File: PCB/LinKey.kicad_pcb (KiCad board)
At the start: 2 copper layers, 25 x 43.5 mm, 1 part

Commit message: Release PCB v1
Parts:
- added C1: 2,2u, Capacitor_SMD:C_0805_2012Metric_Pad1.18x1.45mm_HandSolder, F.Cu at (144.5, 86.2)
- added C2: 1F, Capacitor_THT:CP_Radial_D8.0mm_P3.50mm, B.Cu at (146.9, 73.9)
- added C3: 22u, Capacitor_SMD:C_1206_3216Metric_Pad1.33x1.80mm_HandSolder, B.Cu at (158.3, 80.2)
- added C4: 100n, Capacitor_SMD:C_0603_1608Metric_Pad1.08x0.95mm_HandSolder, B.Cu at (157.5, 78.1)
- added C5: 175p, Capacitor_SMD:C_0603_1608Metric_Pad1.08x0.95mm_HandSolder, B.Cu at (161.8, 75.4)
- added C6: 22u, Capacitor_SMD:C_1206_3216Metric_Pad1.33x1.80mm_HandSolder, B.Cu at (157.4, 72.5)
- added C7: 22u, Capacitor_SMD:C_1206_3216Metric_Pad1.33x1.80mm_HandSolder, B.Cu at (146.2, 65.4)
- added C8: 100n, Capacitor_SMD:C_0603_1608Metric_Pad1.08x0.95mm_HandSolder, B.Cu at (149.2, 64.8)
- added D1: BAS_4002A_RPP_E6327, LinKey_Lib_Footprints:BAS4002ARPPE6327, F.Cu at (144.5, 89.8)
- added D8: LED_RGB, LED_SMD:LED_RGB_5050-6, F.Cu at (160.6, 87.0)
- added J2: Conn_01x04, Connector_PinHeader_2.54mm:PinHeader_1x04_P2.54mm_Vertical, F.Cu at (163.8, 64.5)
- added L1: 1uH, Inductor_SMD:L_Coilcraft_XAL5030-XXX, B.Cu at (152.6, 78.4)
- added Q1: MMBT2907ALT1G, Package_TO_SOT_SMD:SOT-23_Handsoldering, B.Cu at (146.4, 89.3)
- added Q2: CSD25402Q3A, Package_SON:VSON-8_3.3x3.3mm_P0.65mm_NexFET, B.Cu at (153.7, 85.4)
- added R1: R, Resistor_SMD:R_0603_1608Metric_Pad0.98x0.95mm_HandSolder, F.Cu at (147.1, 93.2)
- added R10: 18r, Resistor_SMD:R_1206_3216Metric_Pad1.30x1.75mm_HandSolder, B.Cu at (146.2, 85.9)
- added R11: 200r, Resistor_SMD:R_0603_1608Metric_Pad0.98x0.95mm_HandSolder, B.Cu at (142.7, 89.3)
- added R12: 120r, Resistor_SMD:R_0603_1608Metric_Pad0.98x0.95mm_HandSolder, B.Cu at (157.6, 85.9)
- added R13: 10k, Resistor_SMD:R_0603_1608Metric_Pad0.98x0.95mm_HandSolder, B.Cu at (157.6, 84.1)
- added R14: 2k, Resistor_SMD:R_0603_1608Metric_Pad0.98x0.95mm_HandSolder, B.Cu at (150.2, 89.3)
- added R15: 10k, Resistor_SMD:R_0603_1608Metric_Pad0.98x0.95mm_HandSolder, B.Cu at (157.6, 82.3)
- added R16: 100k, Resistor_SMD:R_0603_1608Metric_Pad0.98x0.95mm_HandSolder, B.Cu at (161.1, 82.3)
- added R17: 453k, Resistor_SMD:R_0603_1608Metric_Pad0.98x0.95mm_HandSolder, B.Cu at (160.0, 75.4)
- added R18: 100k, Resistor_SMD:R_0603_1608Metric_Pad0.98x0.95mm_HandSolder, B.Cu at (160.9, 78.1)
- added R2: R, Resistor_SMD:R_0603_1608Metric_Pad0.98x0.95mm_HandSolder, F.Cu at (148.0, 90.7)
- added R3: R, Resistor_SMD:R_0603_1608Metric_Pad0.98x0.95mm_HandSolder, F.Cu at (143.7, 93.2)
- added R4: 470r, Resistor_SMD:R_0603_1608Metric_Pad0.98x0.95mm_HandSolder, F.Cu at (150.5, 93.3)
- added R5: 10k, Resistor_SMD:R_0603_1608Metric_Pad0.98x0.95mm_HandSolder, F.Cu at (143.7, 83.3)
- added R6: 120r, Resistor_SMD:R_0603_1608Metric_Pad0.98x0.95mm_HandSolder, F.Cu at (160.6, 83.3)
- added R7: 10k, Resistor_SMD:R_0603_1608Metric_Pad0.98x0.95mm_HandSolder, B.Cu at (143.2, 66.2)
- added R8: 330r, Resistor_SMD:R_0603_1608Metric_Pad0.98x0.95mm_HandSolder, F.Cu at (154.3, 87.0)
- added R9: 120r, Resistor_SMD:R_0603_1608Metric_Pad0.98x0.95mm_HandSolder, F.Cu at (154.3, 85.3)
- added REF**: LayerMarker_4_6.35x2.54mm_TextH1mm_P1.27mm_BottomMirrored, Symbol:LayerMarker_4_6.35x2.54mm_TextH1mm_P1.27mm_BottomMirrored, F.Cu at (157.2, 63.2)
- added REF**: MountingHole_2.2mm_M2, MountingHole:MountingHole_2.2mm_M2, F.Cu at (154.3, 90.5)
- added SW2: ~, LinKey_Lib_Footprints:B3U-1000P, F.Cu at (163.8, 78.6)
- added U1: ACPL-214-500E, Package_SO:SOP-4_4.4x2.6mm_P1.27mm, F.Cu at (150.3, 88.0)
- added U2: ESP32-WROOM-32E, RF_Module:ESP32-WROOM-32E, F.Cu at (152.1, 69.0)
- added U4: TL431DBZ, Package_TO_SOT_SMD:SOT-23, B.Cu at (161.4, 85.0)
- added U5: TPS61022, Package_DFN_QFN:Texas_RWU0007A_VQFN-7_2x2mm_P0.5mm, B.Cu at (157.4, 75.4)
- J1: moved to B.Cu
- moved J1 19.0 mm to (144.5, 96.0), turned to 180 degrees
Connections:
- J1 pad 1: unconnected-(J1-A-Pad1) -> Net-(D1-~_2)
- J1 pad 2: unconnected-(J1-I2-Pad2) -> Net-(D1-~_1)
- J1 pad 3: unconnected-(J1-I1-Pad3) -> Net-(J1-I1)
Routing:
- net GND: track 0.00 -> 20.0 mm, vias 0 -> 31
- net Net-(D1-~_1): track 0.00 -> 17.0 mm
- net VCAP: track 0.00 -> 16.8 mm, vias 0 -> 6
- net Net-(Q1-C): track 0.00 -> 15.0 mm
- net Net-(Q2-S): track 0.00 -> 13.7 mm
- net Net-(U4-K): track 0.00 -> 11.9 mm
- net /TIC: track 0.00 -> 11.0 mm
- net /LED_RED: track 0.00 -> 10.7 mm
- net Net-(D8-RA): track 0.00 -> 7.89 mm
- net Net-(Q1-B): track 0.00 -> 7.68 mm
- net Net-(D1-~_2): track 0.00 -> 7.09 mm
- net /LED_GREEN: track 0.00 -> 6.56 mm
- net Net-(J1-I1): track 0.00 -> 5.61 mm
- net Net-(U5-FB): track 0.00 -> 5.29 mm
- net VDD: track 0.00 -> 5.20 mm, vias 0 -> 4
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- added copper zone on B.Cu, net +3.3V
- added copper zone on In2.Cu, net +3.3V
- added copper zone on B.Cu, net GND
- added copper zone on F.Cu, net GND
- added copper zone on In1.Cu, net GND
- added copper zone on B.Cu, net Net-(U5-SW)
- added copper zone on B.Cu, net VCAP
- added copper zone on B.Cu, net VDD
- added copper zone on F.Cu, net VDD
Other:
- board size 25 x 43.5 mm -> 25 x 37.3 mm
- copper layers 2 -> 4
- board text added: "+"
- board text added: "-"
- board text added: "A"
- board text added: "I1"
- board text added: "I2"
- board text added: "Linkey ESP32 01.2026 v1"
- board text added: "R"
- board text added: "T"

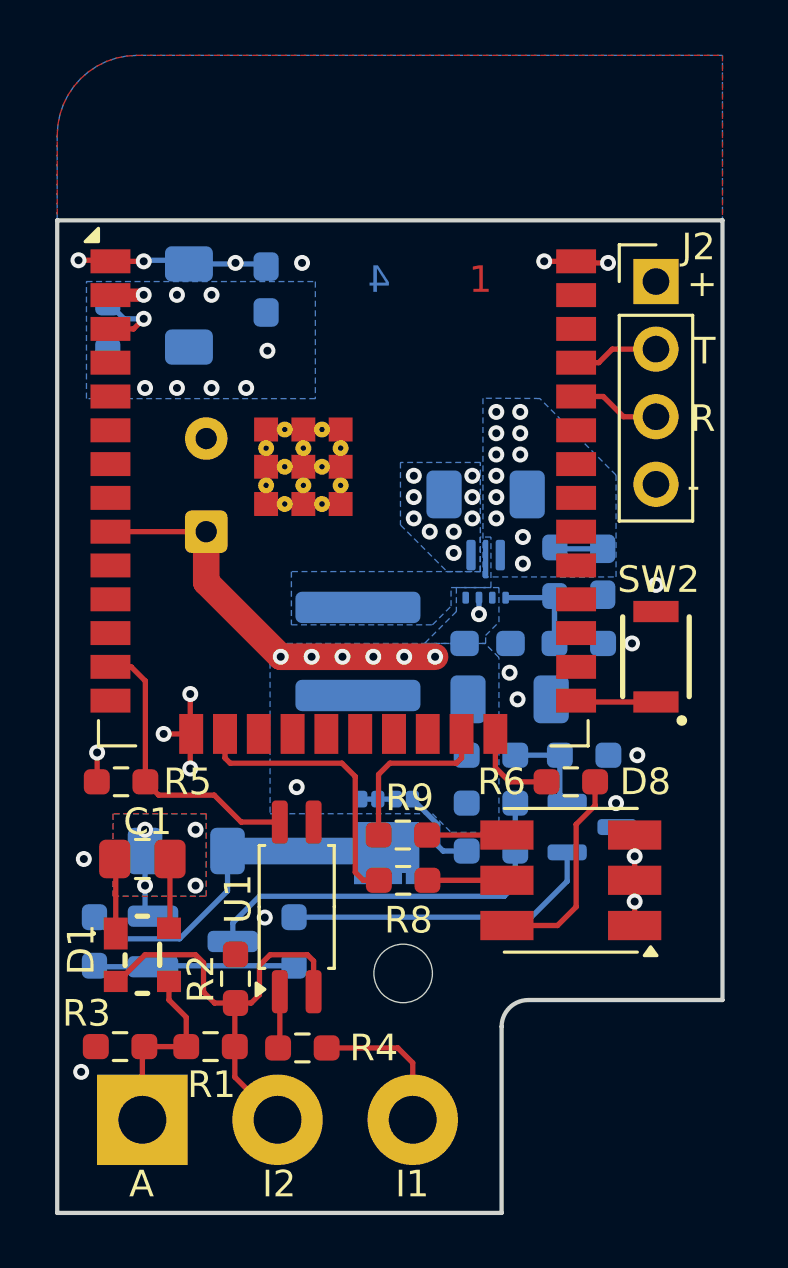
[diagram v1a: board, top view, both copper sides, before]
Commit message: Update pcb version to v1.1
- Fix R10 footprint (was 1206 but should be 0805), decrease value to increase max current to 40mA
- Change R15/R16 values (divided by 10)
- Increase R11 from 200r to 1k to fix voltage limitation
- Fix I1/I2 swap
- Modify R4, R5 values around opto
- Add SW + Capa on EN
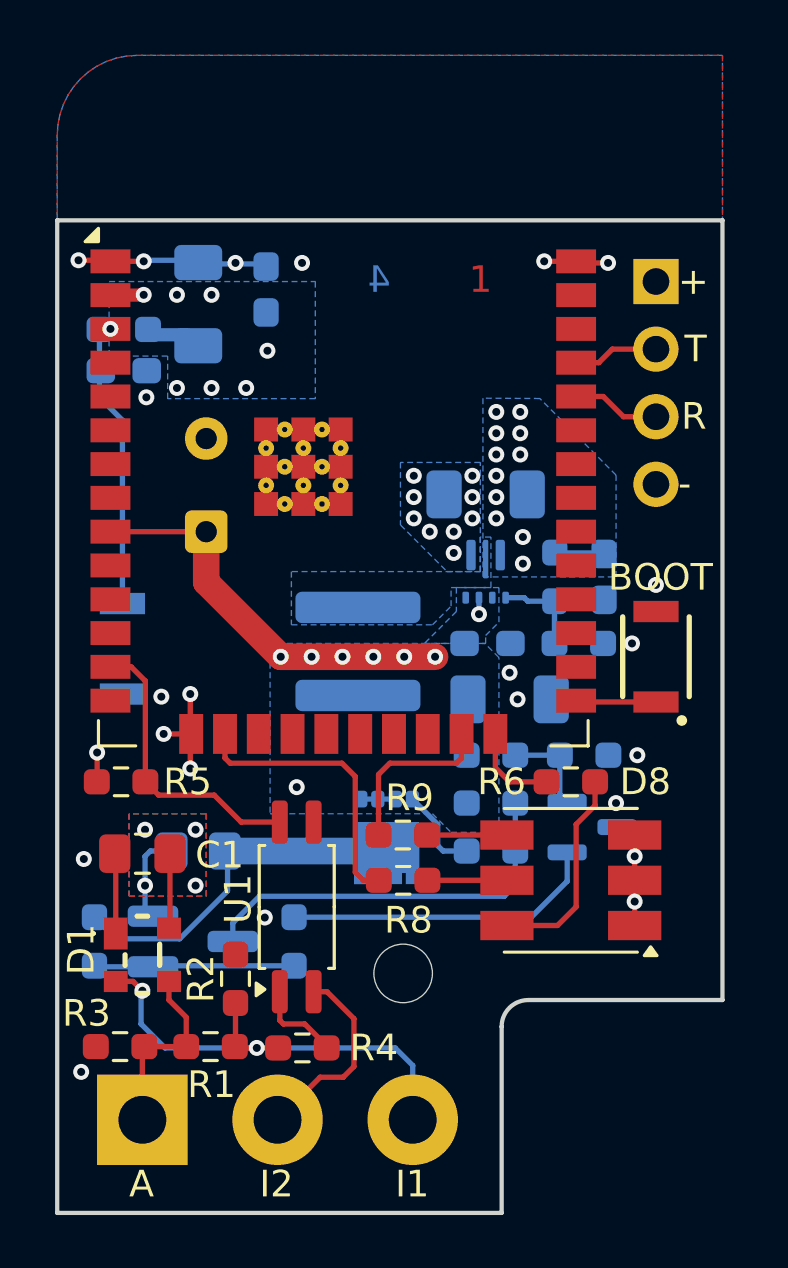
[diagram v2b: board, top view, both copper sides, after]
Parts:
- added C9: 100n, Capacitor_SMD:C_0603_1608Metric_Pad1.08x0.95mm_HandSolder, B.Cu at (143.8, 67.8)
- added SW1: ~, LinKey_Lib_Footprints:B3U-1000P, B.Cu at (143.8, 78.3)
- J2: moved to B.Cu
- R10: value 18r -> 10r; footprint Resistor_SMD:R_1206_3216Metric_Pad1.30x1.75mm_HandSolder -> Resistor_SMD:R_0805_2012Metric_Pad1.20x1.40mm_HandSolder
- R11: value 200r -> 1k
- R15, R5: value 10k -> 1k
- R16: value 100k -> 10k
- R4: value 470r -> 330r
- moved R7 0.61 mm to (143.8, 66.3), turned to 180 degrees
- moved R10 0.45 mm to (146.6, 85.9)
- moved C7 0.35 mm to (146.6, 65.3)
- moved C5 0.20 mm to (161.8, 75.6)
- moved C1 0.20 mm to (144.5, 86.0)
- moved R17 0.19 mm to (160.0, 75.6)
- turned J2 to 180 degrees
- turned R4 to 0 degrees
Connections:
- J1 pad 2: Net-(D1-~_1) -> Net-(J1-I2)
- J1 pad 3: Net-(J1-I1) -> Net-(D1-~_1)
- R4 pad 1: Net-(J1-I1) -> Net-(D1-~_1)
- U1 pad 2: Net-(D1-~_1) -> Net-(J1-I2)
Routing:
- net Net-(U2-EN): track 2.87 -> 10.7 mm
- net Net-(J1-I2): track 0.00 -> 7.43 mm
- net Net-(J1-I1): track 5.61 -> 0.00 mm
- net +3.3V: track 4.44 -> 6.68 mm, vias 20 -> 19
- net Net-(D1-~_1): track 17.0 -> 18.8 mm, vias 0 -> 2
- net Net-(R4-Pad2): track 2.14 -> 3.31 mm
- net VDD: track 5.20 -> 6.08 mm
- net GND: track 20.0 -> 20.4 mm, vias 31 -> 33
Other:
- board text added: "BOOT"
- board text added: "Linkey ESP32 02.2026 v1.1"
- board text added: "RST"
- board text removed: "Linkey ESP32 01.2026 v1"

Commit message: Update R11 position and J1's 3D model
- Slightly move R11 away from the PCB edge
- Add J1's 3D model
- Complete J1's BOM data = Samtech vertical header that must be manually bent
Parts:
- moved R11 0.21 mm to (142.9, 89.3)
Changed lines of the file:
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@@
 			)
 		)
-		(property "Datasheet" "~"
+		(property "Datasheet" "https://suddendocs.samtec.com/catalog_english/hpm.pdf?_gl=1*mr8nsh*_up*MQ..*_ga*NTc2NzY4MDc5LjE3NDAyMzU5NjI.*_ga_3KFNZC07WW*czE3NzU1OTQ0MDckbzIkZzAkdDE3NzU1OTQ0MDckajYwJGwwJGg2MDEyMTQ0MzQ."
 			(at 0 0 0)
 			(unlocked yes)
@@
 			)
 		)
+		(property "Manufacturer_Name" "Samtec"
+			(at 0 0 180)
+			(unlocked yes)
+			(layer "B.Fab")
+			(hide yes)
+			(effects
+				(font
+					(size 1 1)
+					(thickness 0.15)
+				)
+				(justify mirror)
+			)
+		)
+		(property "Manufacturer_Part_Number" "HPM-03-04-T-S "
+			(at 0 0 180)
+			(unlocked yes)
+			(layer "B.Fab")
+			(hide yes)
+			(effects
+				(font
+					(size 1 1)
+					(thickness 0.15)
+				)
+				(justify mirror)
+			)
+		)
+		(property "Supplier1_Name" "Mouser"
+			(at 0 0 180)
+			(unlocked yes)
+			(layer "B.Fab")
+			(hide yes)
+			(effects
+				(font
+					(size 1 1)
+					(thickness 0.15)
+				)
+				(justify mirror)
+			)
+		)
+		(property "Supplier1_Part_Number" "200-HPM0304TS "
+			(at 0 0 180)
+			(unlocked yes)
+			(layer "B.Fab")
+			(hide yes)
+			(effects
+				(font
+					(size 1 1)
+					(thickness 0.15)
+				)
+				(justify mirror)
+			)
+		)
 		(property ki_fp_filters "Connector*:*_1x??_*")
 		(sheetname "/")
@@
 		)
 		(embedded_fonts no)
-		(model "${KIPRJMOD}/3D step files/Conn_01x03.step"
+		(model "${KIPRJMOD}/MCAD files/3D step files/Conn_01x03.step"
 			(offset
 				(xyz 0 0 -2.5)
@@
 		(tags "SOT TO_SOT_SMD")
 		(property "Reference" "U4"
-			(at -0.1 2.5 0)
+			(at -0.1 2.5 90)
 			(layer "B.SilkS")
 			(effects
@@
 			)
 		)
-		(property "Description" "Generic connector, single row, 01x04, script generated (kicad-library-utils/schlib/autogen/connector/)"
+		(property "Description" "Headers & Wire Housings .200 Power Terminal Strip"
 			(at 0 0 0)
 			(layer "B.Fab")
@@
 		(tags "resistor handsolder")
 		(property "Reference" "R12"
-			(at 0 4 0)
+			(at 0 4 90)
 			(layer "B.SilkS")
 			(effects
@@
 	(footprint "Resistor_SMD:R_0603_1608Metric_Pad0.98x0.95mm_HandSolder"
 		(layer "B.Cu")
-		(at 142.7 89.3 -90)
+		(at 142.91 89.3 -90)
 		(descr "Resistor SMD 0603 (1608 Metric), square (rectangular) end terminal, IPC-7351 nominal with elongated pad for handsoldering. (Body size source: IPC-SM-782 page 72, https://www.pcb-3d.com/wordpress/wp-content/uploads/ipc-sm-782a_amendment_1_and_2.pdf), generated with kicad-footprint-generator")
 		(tags "resistor handsolder")
@@
 	)
 	(segment
+		(start 142.9175 90.25)
+		(end 142.91 90.2425)
+		(width 0.2)
+		(layer "B.Cu")
+		(net 48)
+	)
+	(segment
 		(start 150.2 90.2125)
 		(end 144.9375 90.2125)
@@
 	)
 	(segment
+		(start 142.91 90.2425)
+		(end 142.73 90.2425)
+		(width 0.2)
+		(layer "B.Cu")
+		(net 48)
+	)
+	(segment
 		(start 144.9375 90.2125)
 		(end 144.9 90.25)
@@
 	(segment
 		(start 144.9 90.25)
-		(end 142.7375 90.25)
+		(end 142.9175 90.25)
 		(width 0.2)
 		(layer "B.Cu")
@@
 	)
 	(segment
-		(start 142.7375 90.25)
+		(start 142.73 90.2425)
 		(end 142.7 90.2125)
 		(width 0.2)
@@
 	)
 	(segment
-		(start 145.9 89.2)
-		(end 147.7 87.4)
+		(start 142.91 88.4175)
+		(end 143.6925 89.2)
 		(width 0.2)
 		(layer "B.Cu")
@@
 	)
 	(segment
-		(start 142.95 88.4)
-		(end 143 88.45)
+		(start 147.7 87.4)
+		(end 147.7 85.9)
 		(width 0.2)
 		(layer "B.Cu")
@@
 	)
 	(segment
-		(start 143.5125 89.2)
-		(end 145.9 89.2)
+		(start 142.95 88.4)
+		(end 143 88.45)
 		(width 0.2)
 		(layer "B.Cu")
@@
 	)
 	(segment
-		(start 142.7 88.3875)
-		(end 143.5125 89.2)
+		(start 145.9 89.2)
+		(end 147.7 87.4)
 		(width 0.2)
 		(layer "B.Cu")
@@
 	)
 	(segment
-		(start 147.7 87.4)
-		(end 147.7 85.9)
+		(start 143.6925 89.2)
+		(end 145.9 89.2)
 		(width 0.2)
 		(layer "B.Cu")
